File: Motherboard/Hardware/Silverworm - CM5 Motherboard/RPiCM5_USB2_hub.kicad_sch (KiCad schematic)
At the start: 4 parts, among them IC1 CY7C65632-28LTXC, J1 USB_A_Stacked, J13 USB_A_Stacked

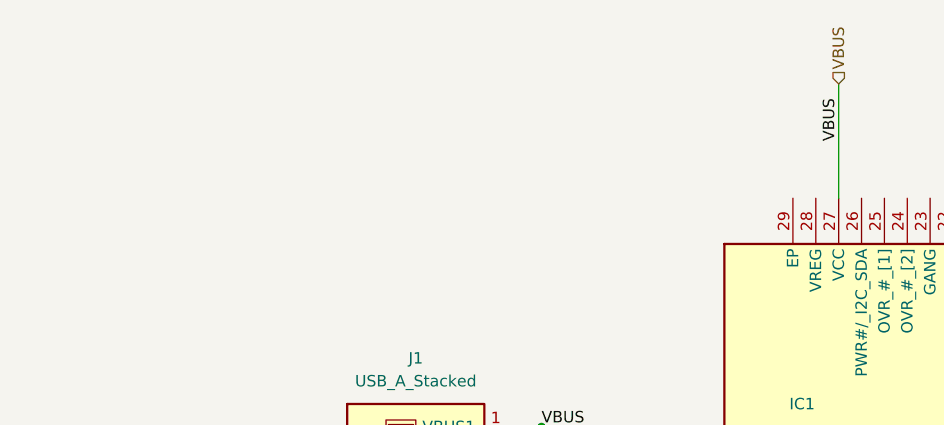
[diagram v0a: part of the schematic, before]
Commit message: Added footprints and board connectors
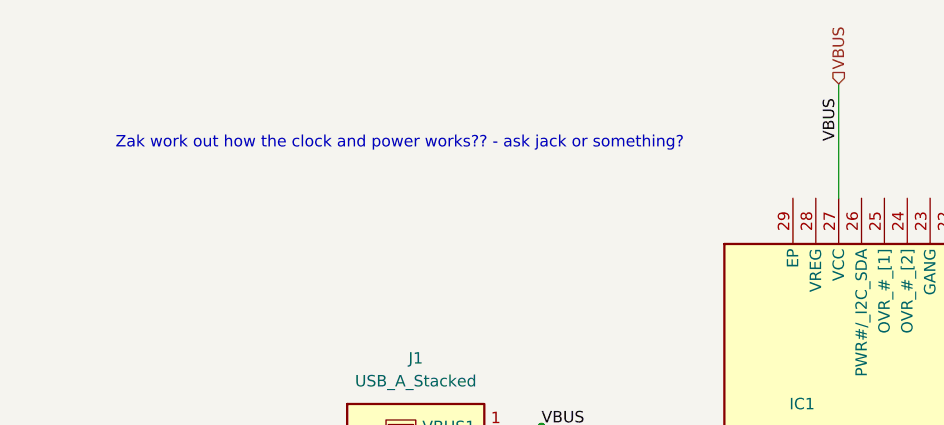
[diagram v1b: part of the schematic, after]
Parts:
- IC1: footprint QFN50P500X500X80-29N-D -> CM5IO:QFN50P500X500X80-29N-D
- J1, J13: footprint (none) -> CM5IO:57876171
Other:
- note added: "Zak work out how the clock and power works?? - ask jack or something?"
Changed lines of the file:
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@@
 		(comment 1 "DMT4 - Silerworm, Group 4C")
+	)
+	(text "Zak work out how the clock and power works?? - ask jack or something?"
+		(exclude_from_sim no)
+		(at 118.872 57.404 0)
+		(effects
+			(font
+				(size 1.27 1.27)
+			)
+		)
 	)
 	(junction
@@
 			)
 		)
-		(property "Footprint" ""
+		(property "Footprint" "CM5IO:57876171"
 			(at 226.06 132.08 0)
 			(effects
@@
 			)
 		)
-		(property "Footprint" "QFN50P500X500X80-29N-D"
+		(property "Footprint" "CM5IO:QFN50P500X500X80-29N-D"
 			(at 189.23 166.04 0)
 			(effects
@@
 			)
 		)
-		(property "Footprint" ""
+		(property "Footprint" "CM5IO:57876171"
 			(at 124.46 113.03 0)
 			(effects

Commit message: Layout and IO edits
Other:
- title: Compute Module 5 IO Board - Top Level -> Silverworm CM5 Motherboard - USB 2.0 Hub
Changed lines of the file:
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@@
 	(paper "A4")
 	(title_block
-		(title "Compute Module 5 IO Board - Top Level")
+		(title "Silverworm CM5 Motherboard - USB 2.0 Hub")
 		(date "2026-01-27")
 		(company "Copyright © Zak Leek, Imperial College London")
@@
 	(text "Zak work out how the clock and power works?? - ask jack or something?"
 		(exclude_from_sim no)
-		(at 118.872 57.404 0)
+		(at 116.332 74.93 0)
 		(effects
 			(font

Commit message: PCB changes (many)
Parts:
- added J20: USB_A, molex_usb:CONN_48204-0001_MOL, symbol Connector:USB_A
- IC1: now not fitted; now left out of the parts list
- J21: renamed from J1; now not fitted; now left out of the parts list
- J22: renamed from J13; now not fitted; now left out of the parts list
- R24: renamed from R20; now not fitted; now left out of the parts list
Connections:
- net D+: now also J20.3 (D+)
- net D-: now also J20.2 (D-)
- net GND: now also J20.4 (GND), J20.5 (Shield)
- net VBUS: now also J20.1 (VBUS)
